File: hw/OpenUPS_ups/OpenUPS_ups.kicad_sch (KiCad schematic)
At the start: 15 parts, among them J101 XT60PW-M, J102 Barrel Jack, J103 Screw Terminal, J104 Screw Terminal, J105 Screw Terminal, J106 JST XH, J107 JST XH, U102 AVR32DB48x-xPT

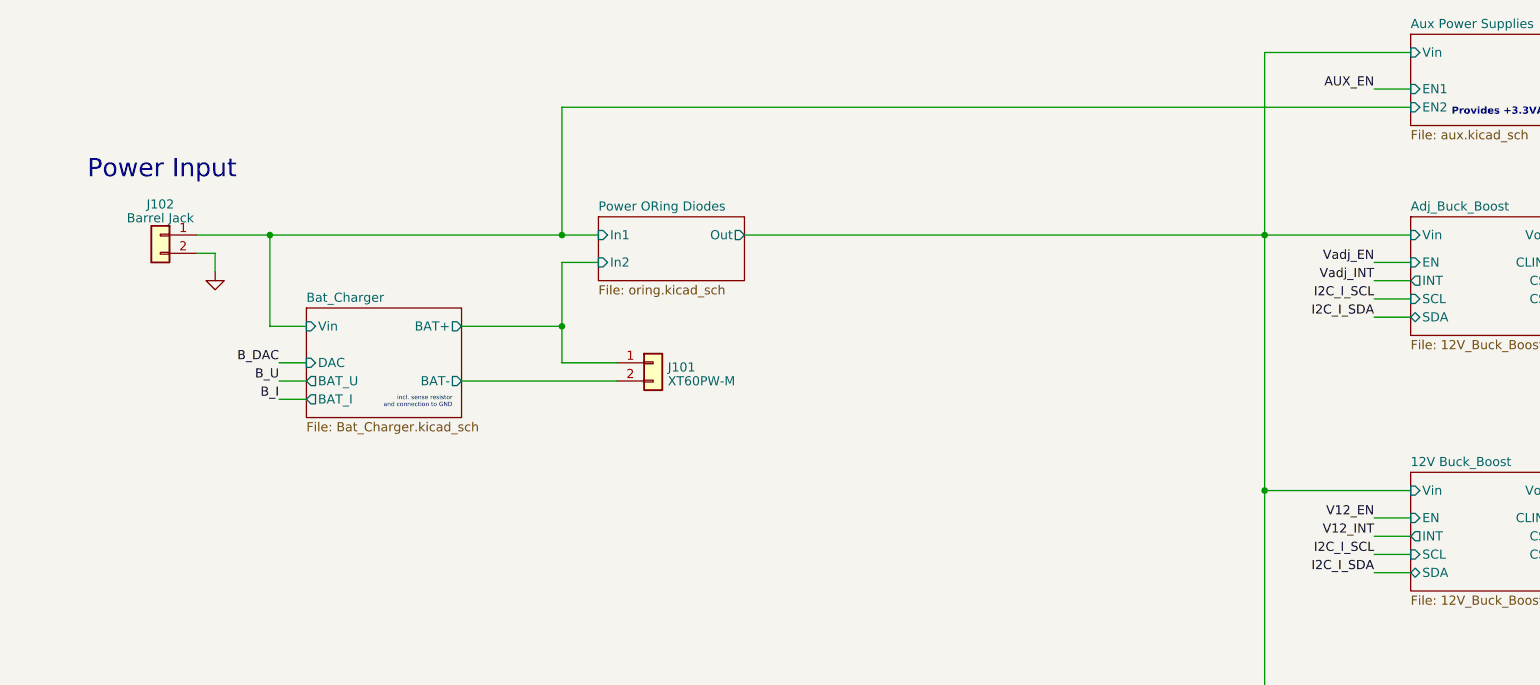
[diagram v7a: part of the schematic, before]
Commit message: Issue #24 5th generation charger (may need some tuning)
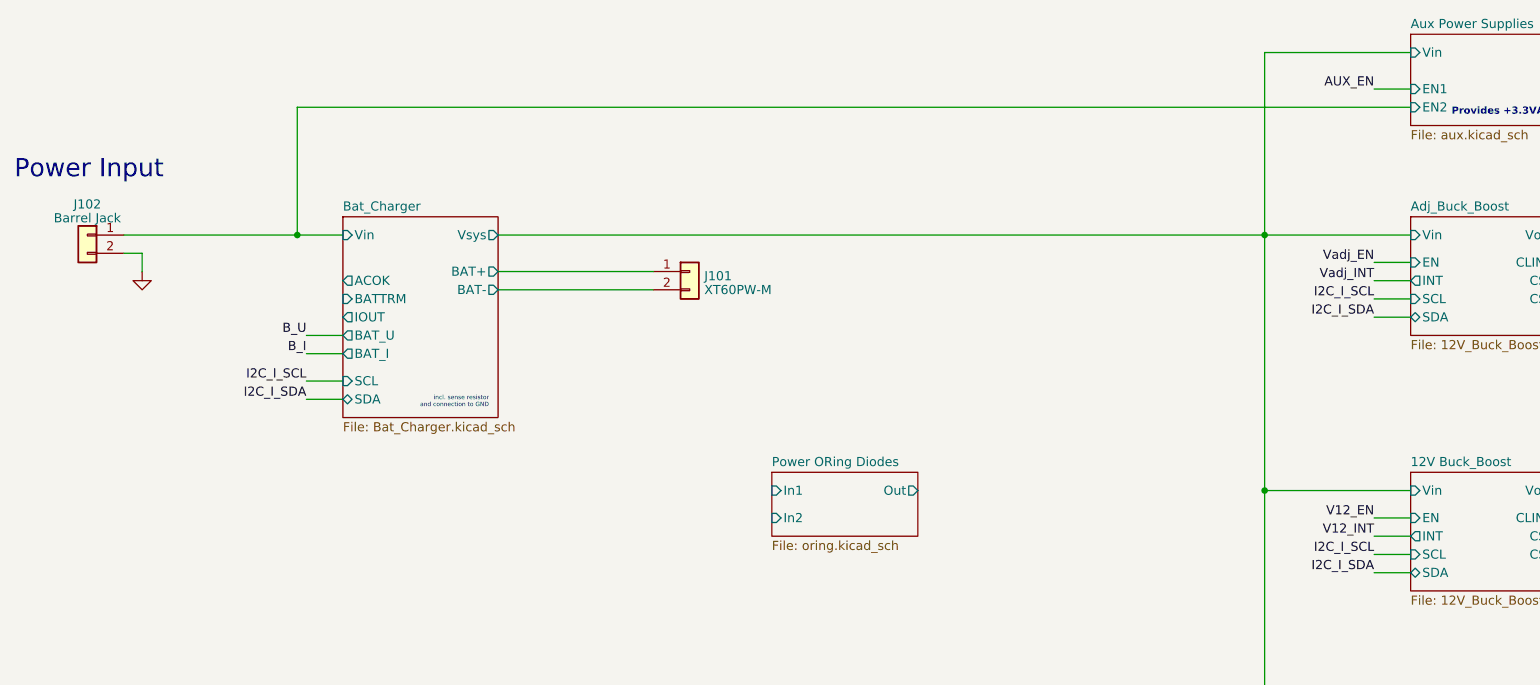
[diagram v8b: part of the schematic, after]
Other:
- sheet Bat_Charger ports: added ACOK, BATTRM, IOUT, SCL, SDA, Vsys; removed DAC
- moved on the sheet: J101, J102
